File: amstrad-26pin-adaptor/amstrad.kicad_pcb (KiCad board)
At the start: 2 copper layers, 48.3 x 19.7 mm, 2 parts, among them P1 FLOPPY_34, P2 FLOPPY_26

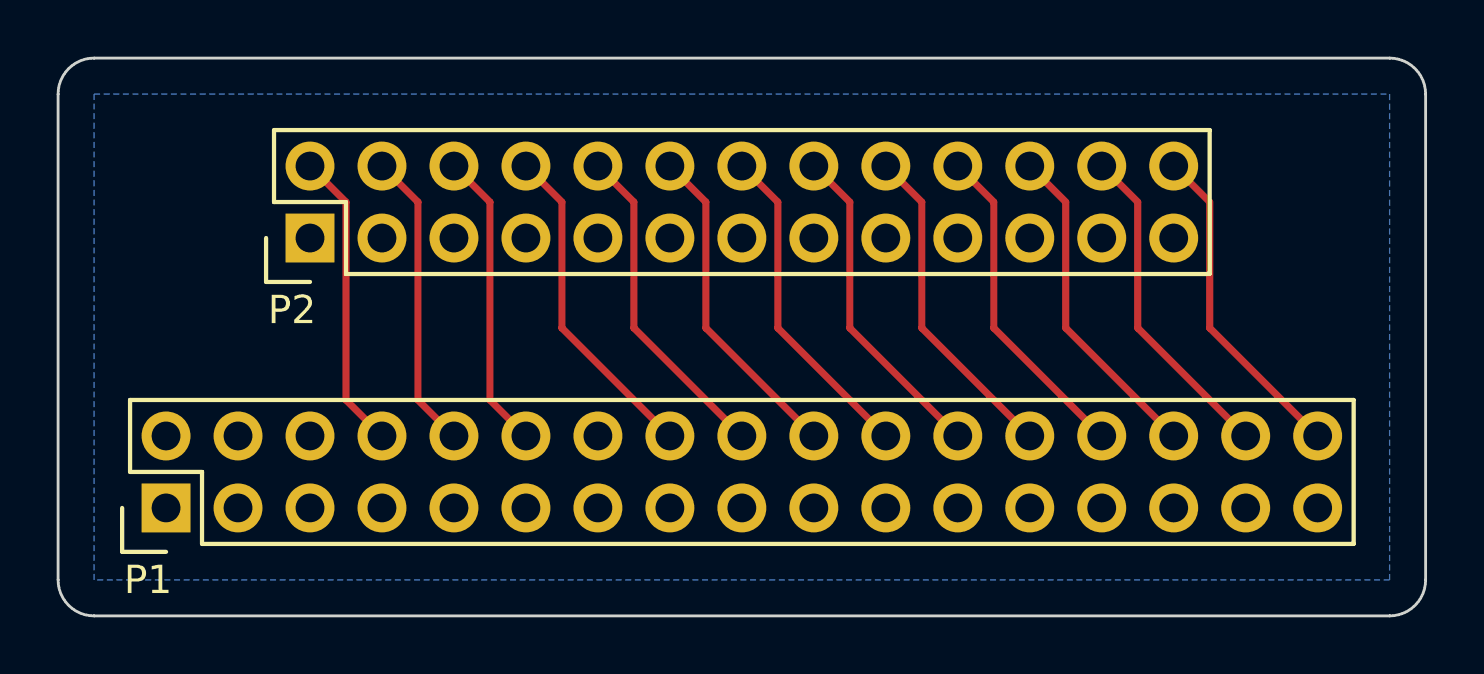
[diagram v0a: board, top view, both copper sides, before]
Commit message: New panelisation of the 27c400 adaptor + amstrad adaptor, 2 up. Place panelisations in their own folder. Fold Amstrad silks changes into the base amstrad layout file.
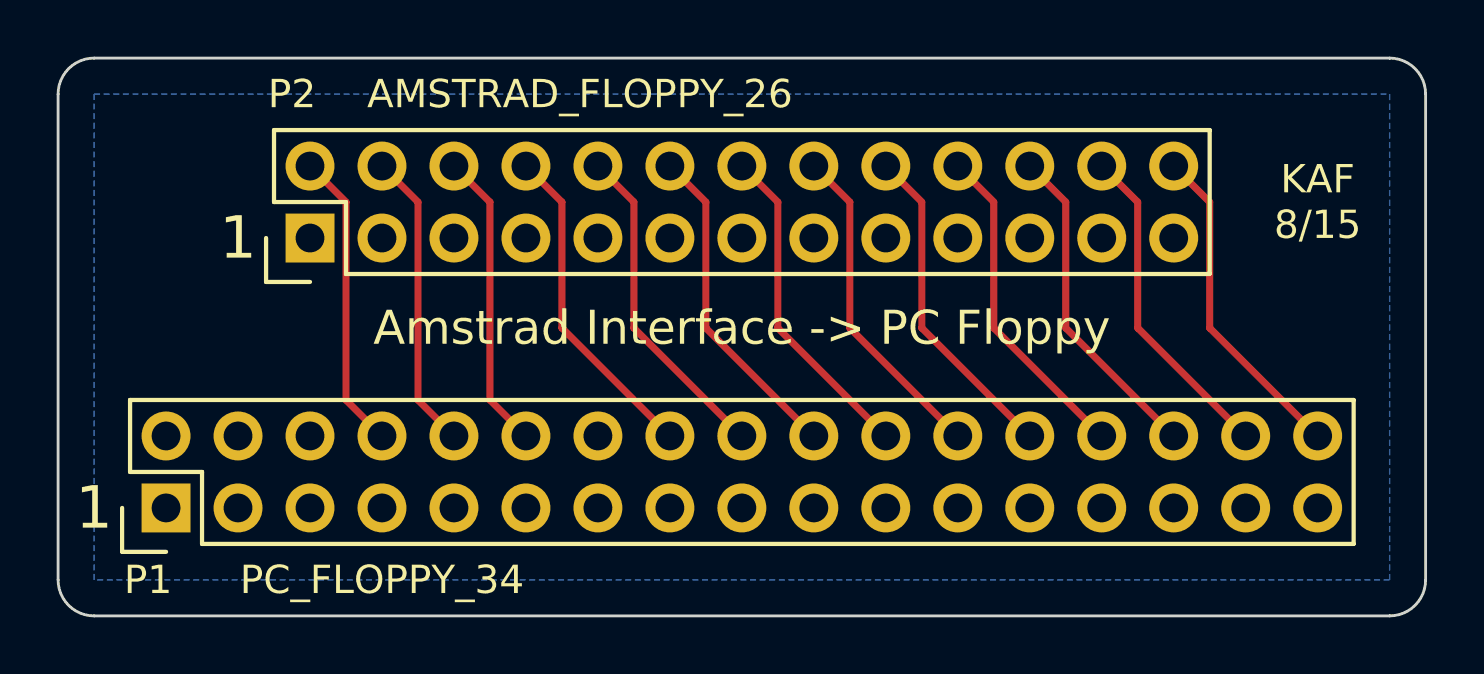
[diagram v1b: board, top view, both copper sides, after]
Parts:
- P1: value FLOPPY_34 -> PC_FLOPPY_34
- P2: value FLOPPY_26 -> AMSTRAD_FLOPPY_26
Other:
- board text added: "1"
- board text added: "Amstrad Interface -> PC Floppy"
- board text added: "KAF 8/15"
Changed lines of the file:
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@@
     (links 42)
     (no_connects 0)
-    (area 119.964999 93.929999 168.325001 112.445001)
+    (area 119.964999 93.929999 168.325001 113.715001)
     (thickness 1.6)
-    (drawings 8)
+    (drawings 12)
     (tracks 39)
     (zones 0)
@@
       (effects (font (size 1 1) (thickness 0.15)))
     )
-    (fp_text value FLOPPY_34 (at -2.54 7.62 180) (layer F.Fab)
+    (fp_text value PC_FLOPPY_34 (at -2.54 7.62 180) (layer F.SilkS)
       (effects (font (size 1 1) (thickness 0.15)))
     )
@@
     (descr "Through hole pin header")
     (tags "pin header")
-    (fp_text reference P2 (at -2.54 -0.635 180) (layer F.SilkS)
+    (fp_text reference P2 (at 5.08 -0.635 180) (layer F.SilkS)
       (effects (font (size 1 1) (thickness 0.15)))
     )
-    (fp_text value FLOPPY_26 (at -2.54 7.62 180) (layer F.Fab)
+    (fp_text value AMSTRAD_FLOPPY_26 (at 5.08 9.525 180) (layer F.SilkS)
       (effects (font (size 1 1) (thickness 0.15)))
     )
@@
     )
   )
+  (gr_text "KAF\n8/15" (at 164.465 99.06) (layer F.SilkS)
+    (effects (font (size 1 1) (thickness 0.15)))
+  )
+  (gr_text "Amstrad Interface -> PC Floppy" (at 144.145 103.505) (layer F.SilkS)
+    (effects (font (size 1.2 1.2) (thickness 0.2)))
+  )
+  (gr_text 1 (at 121.285 109.855) (layer F.SilkS)
+    (effects (font (size 1.5 1.5) (thickness 0.2)))
+  )
+  (gr_text 1 (at 126.365 100.33) (layer F.SilkS)
+    (effects (font (size 1.5 1.5) (thickness 0.2)))
+  )
   (gr_line (start 121.285 93.98) (end 167.005 93.98) (angle 90) (layer Edge.Cuts) (width 0.1))

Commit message: amstrad-26: Clean up board silks
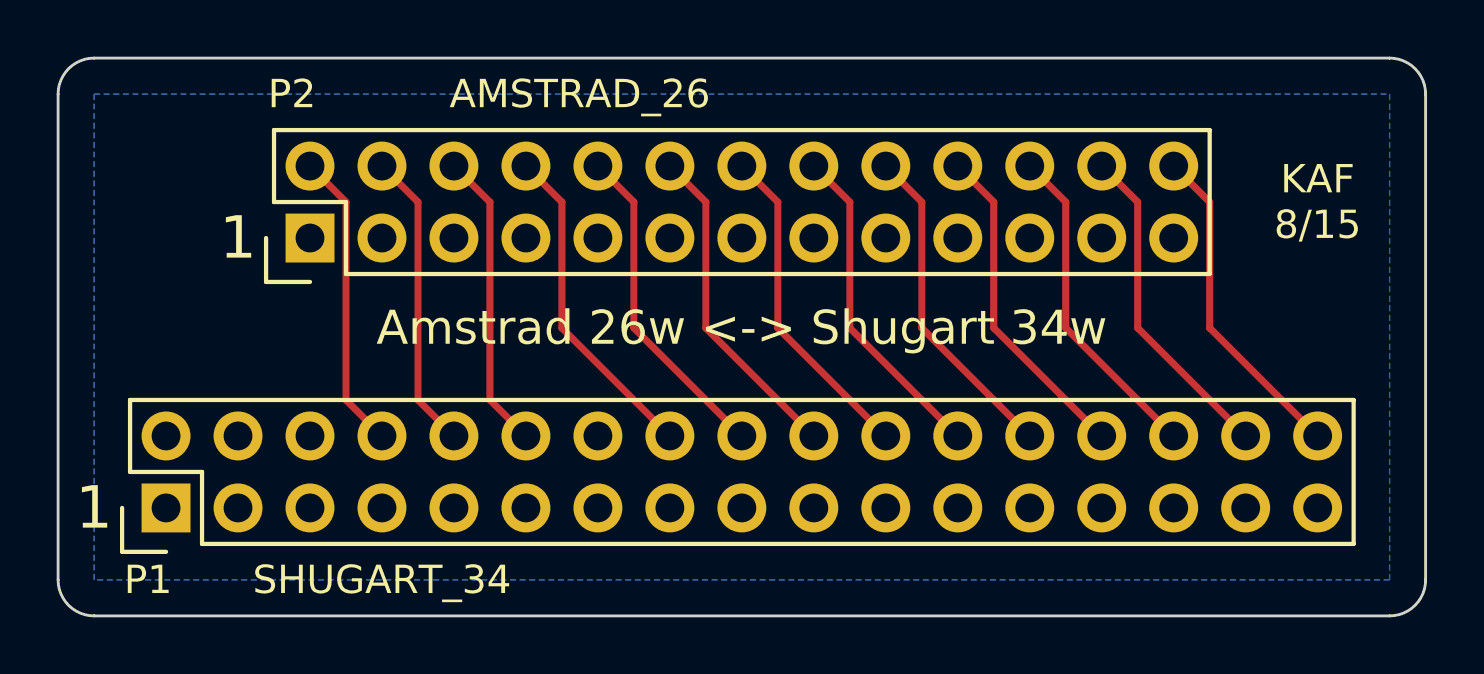
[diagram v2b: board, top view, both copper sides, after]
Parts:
- P1: value PC_FLOPPY_34 -> SHUGART_34
- P2: value AMSTRAD_FLOPPY_26 -> AMSTRAD_26
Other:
- board text added: "Amstrad 26w <-> Shugart 34w"
- board text removed: "Amstrad Interface -> PC Floppy"
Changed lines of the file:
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@@
-(kicad_pcb (version 4) (host pcbnew "(after 2015-may-25 BZR unknown)-product")
+(kicad_pcb (version 20171130) (host pcbnew 5.0.2-bee76a0~70~ubuntu18.04.1)
   (general
-    (links 42)
-    (no_connects 0)
-    (area 119.964999 93.929999 168.325001 113.715001)
     (thickness 1.6)
     (drawings 12)
@@
     (pad_drill 0.6)
     (pad_to_mask_clearance 0)
+    (solder_mask_min_width 0.25)
     (aux_axis_origin 0 0)
     (visible_elements FFFFFF7F)
@@
       (layerselection 0x00030_80000001)
       (usegerberextensions false)
+      (usegerberattributes false)
+      (usegerberadvancedattributes false)
+      (creategerberjobfile false)
       (excludeedgelayer true)
       (linewidth 0.100000)
@@
       (hpglpennumber 1)
       (hpglpenspeed 20)
-      (hpglpendiameter 15)
-      (hpglpenoverlay 2)
+      (hpglpendiameter 15.000000)
       (psnegative false)
       (psa4output false)
@@
       (effects (font (size 1 1) (thickness 0.15)))
     )
-    (fp_text value PC_FLOPPY_34 (at -2.54 7.62 180) (layer F.SilkS)
+    (fp_text value SHUGART_34 (at -2.54 7.62 180) (layer F.SilkS)
       (effects (font (size 1 1) (thickness 0.15)))
     )
@@
       (net 18 /RDY))
     (model Pin_Headers.3dshapes/Pin_Header_Straight_2x17.wrl
-      (at (xyz 0.05 -0.8 0))
+      (offset (xyz 1.269999980926514 -20.31999969482422 0))
       (scale (xyz 1 1 1))
       (rotate (xyz 0 0 90))
@@
       (effects (font (size 1 1) (thickness 0.15)))
     )
-    (fp_text value AMSTRAD_FLOPPY_26 (at 5.08 9.525 180) (layer F.SilkS)
+    (fp_text value AMSTRAD_26 (at 5.08 9.525 180) (layer F.SilkS)
       (effects (font (size 1 1) (thickness 0.15)))
     )
@@
       (net 18 /RDY))
     (model Pin_Headers.3dshapes/Pin_Header_Straight_2x13.wrl
-      (at (xyz 0.05 -0.6 0))
+      (offset (xyz 1.269999980926514 -15.23999977111816 0))
       (scale (xyz 1 1 1))
       (rotate (xyz 0 0 90))
@@
     (effects (font (size 1 1) (thickness 0.15)))
   )
-  (gr_text "Amstrad Interface -> PC Floppy" (at 144.145 103.505) (layer F.SilkS)
+  (gr_text "Amstrad 26w <-> Shugart 34w" (at 144.145 103.505) (layer F.SilkS)
     (effects (font (size 1.2 1.2) (thickness 0.2)))
   )
